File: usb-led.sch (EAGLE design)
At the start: 13 parts, among them U1 Tiny85-20-SMT

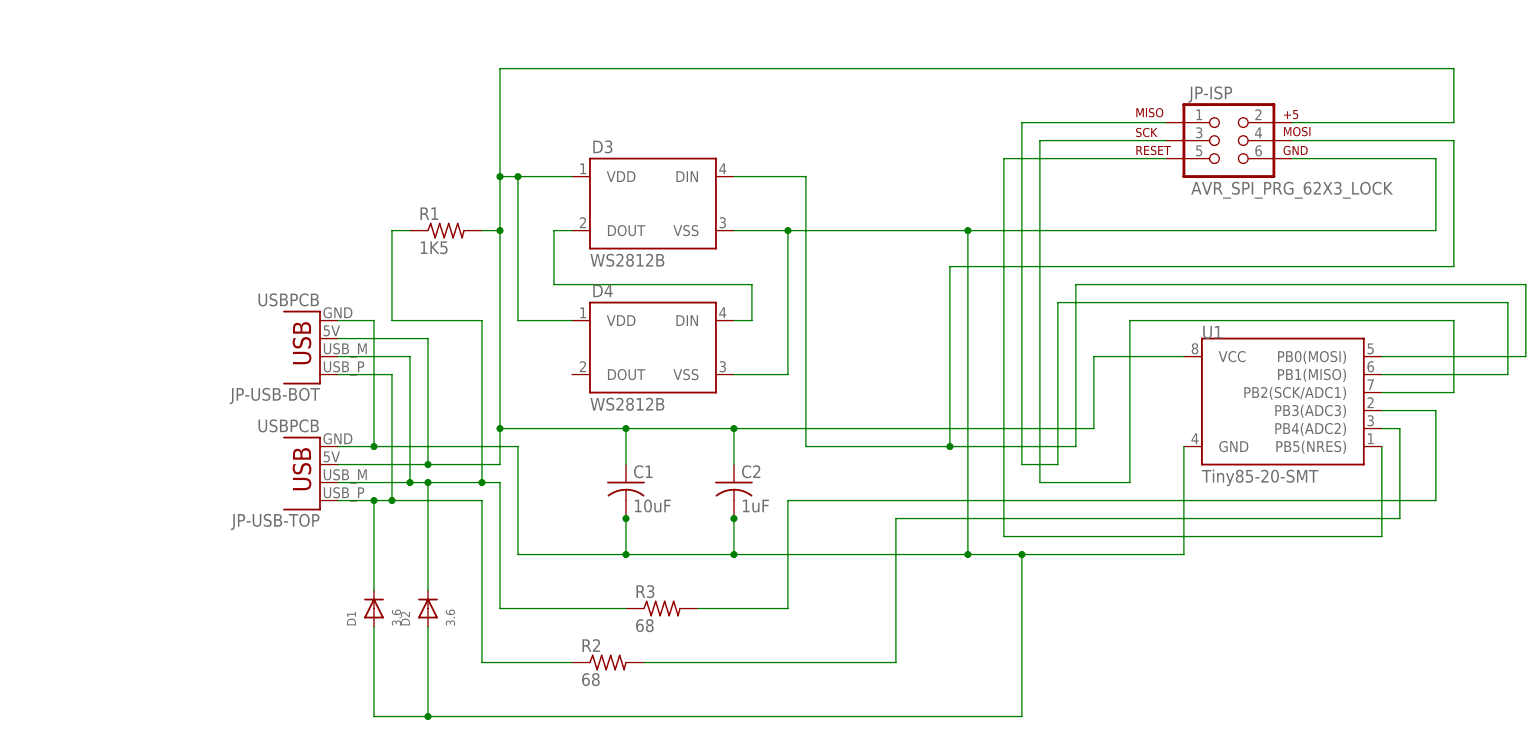
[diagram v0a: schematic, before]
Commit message: Depend on SOIC clip. Add MacroFab dependencies (micro USB).
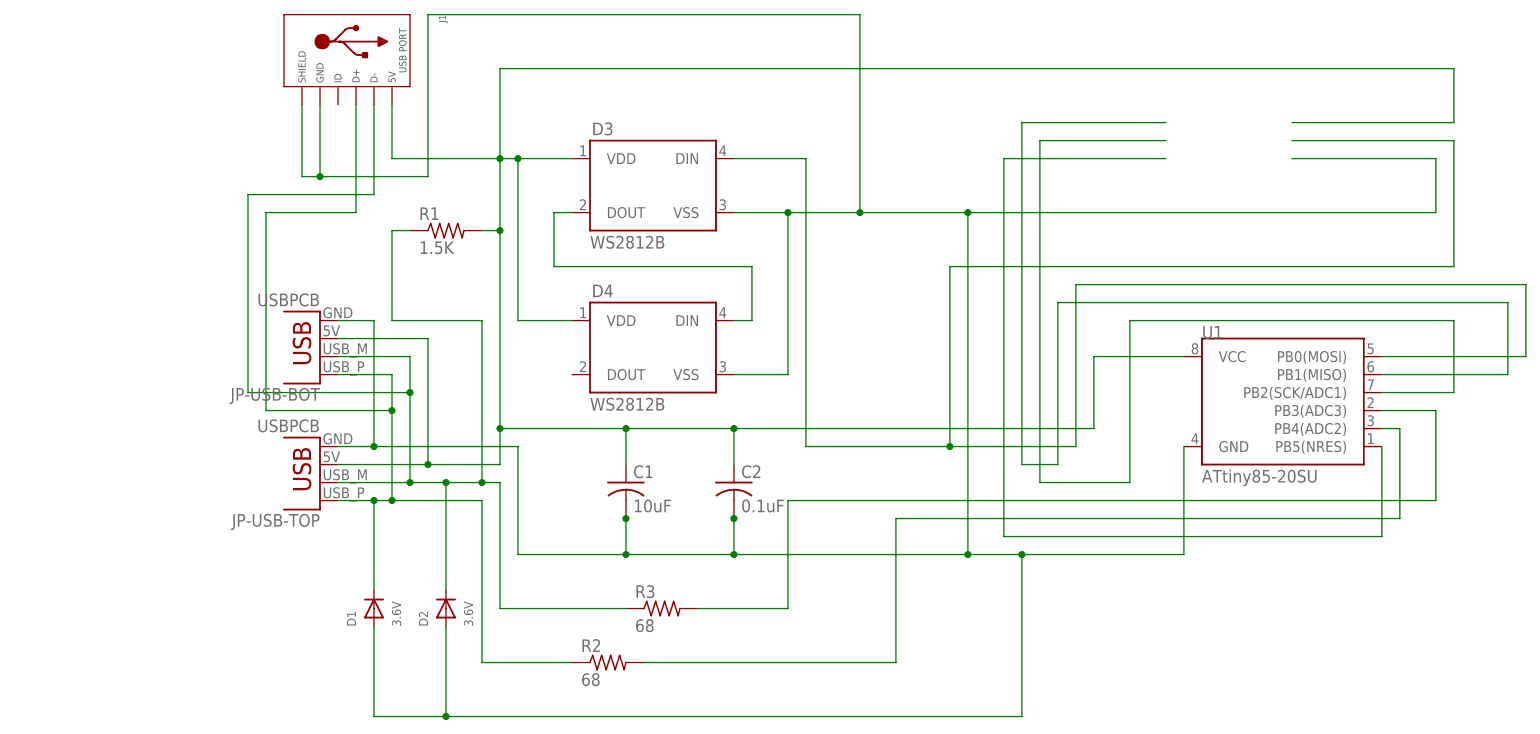
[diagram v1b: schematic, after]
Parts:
- removed JP-ISP: AVR_SPI_PRG_62X3_LOCK, SparkFun-Connectors:AVR_SPI_PRG_62X3_LOCK
- added J1: (no value), MF_Connectors:USB_MICRO_RIGHT
- C1: device rcl:C-USC0805 -> rcl:C-USC0402
- C2: value 1uF -> 0.1uF; device rcl:C-USC0805 -> rcl:C-USC0402
- D1, D2: value 3.6 -> 3.6V; device microbuilder:DIODESOD-323 -> microbuilder:DIODESOD-523
- R1: value 1K5 -> 1.5K; device rcl:R-US_R0805 -> rcl:R-US_R0402
- R2, R3: device rcl:R-US_R0805 -> rcl:R-US_R0402
- U1: value Tiny85-20-SMT -> ATtiny85-20SU
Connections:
- net GND: now also J1.GND, J1.SLD; no longer JP-ISP.6
- net MISO: no longer JP-ISP.1
- net MOSI/DIN: no longer JP-ISP.4
- net RESET: no longer JP-ISP.5
- net SCK: no longer JP-ISP.3
- net USB_D_MINUS_RAW: now also J1.D-
- net USB_D_PLUS_RAW: now also J1.D+
- net VCC: now also J1.5V; no longer JP-ISP.2
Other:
- moved on the sheet: D2, D3

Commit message: mf2.
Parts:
- removed J1: (no value), MF_Connectors:USB_MICRO_RIGHT
- added JP-ISP: AVR_MINI_PROGSMD, SparkFun-Connectors:AVR_MINI_PROGSMD
- added JP-USB-MICRO: (no value), MF_Connectors:USB_MICRO_RIGHT
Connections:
- net GND: now also JP-ISP.GND, JP-USB-MICRO.GND, JP-USB-MICRO.SLD; no longer J1.GND, J1.SLD
- net MISO: now also JP-ISP.MISO
- net MOSI/DIN: now also JP-ISP.MOSI
- net RESET: now also JP-ISP.RST
- net SCK: now also JP-ISP.SCK
- net USB_D_MINUS_RAW: now also JP-USB-MICRO.D-; no longer J1.D-
- net USB_D_PLUS_RAW: now also JP-USB-MICRO.D+; no longer J1.D+
- net VCC: now also JP-ISP.VCC, JP-USB-MICRO.5V; no longer J1.5V
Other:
- moved on the sheet: C1, C2, D1, D2, D3, D4, JP-USB-BOT, JP-USB-TOP, R1, R2, R3, U1
